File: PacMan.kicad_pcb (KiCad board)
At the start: 2 copper layers, 134.6 x 109.2 mm, 163 parts, among them J1 POWER+, J10 SEG+ CellMen, J13 AIR Left, J14 AIR Right, J2 POWER-, J4 Charge Detection, J5 SEG- CellMen, J6 BusBar Current Sensor, J7 Panel, J8 SLOOP, J9 GLV/CAN, K1 G5Q-1A4 DC24, K2 T9AS1D12-24, K3 T9AS1D12-24, Q1 DMN3730U, Q2 DMN3730U, Q4 DMP10H4D2S, Q5 DMP10H4D2S, U1 MCP9804, U10 LTC4151, U11 INA592, U12 MEF1S2405SP3C, U13 V7805-500, U14 Si8600AC, U15 Si8600AC, U16 TEC3-2419, U17 TEC3-2419, U18 AP2204K-5.0, U19 TLP293-4, U2 MCP9804, U21 Si8600AC, U22 AP2204K-5.0, U3 ADM6320, U4 MCP2551-I-SN, U5 ESP32_DEVKITC, U6 MCP23008, U7 BQ32002, U8 ACHS-7122, U9 PDQE10-Q48-S24-D, Y1 32K

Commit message: quick little routing thing
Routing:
- net /MCU/BTN_LEFT_MCU: track 44.4 -> 43.3 mm
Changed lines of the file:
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@@
-(kicad_pcb (version 20171130) (host pcbnew "(5.1.4)-1")
+(kicad_pcb (version 20171130) (host pcbnew "(5.1.5)-3")
   (general
     (thickness 1.6)
     (drawings 77)
-    (tracks 1638)
+    (tracks 1636)
     (zones 0)
     (modules 163)
@@
   )
   (setup
-    (last_trace_width 0.5)
+    (last_trace_width 0.25)
     (user_trace_width 0.5)
     (user_trace_width 1)
@@
     (add_net "Net-(ISO4-Pad1)")
     (add_net "Net-(ISO7-Pad1)")
-    (add_net "Net-(J10-Pad5)")
-    (add_net "Net-(J5-Pad5)")
-    (add_net "Net-(J6-Pad1)")
-    (add_net "Net-(J6-Pad6)")
-    (add_net "Net-(J7-Pad6)")
     (add_net "Net-(R2-Pad1)")
     (add_net "Net-(R24-Pad2)")
@@
     (add_net "Net-(R46-Pad1)")
     (add_net "Net-(R5-Pad1)")
-    (add_net "Net-(U1-Pad3)")
-    (add_net "Net-(U10-Pad8)")
-    (add_net "Net-(U11-Pad8)")
-    (add_net "Net-(U16-Pad3)")
-    (add_net "Net-(U17-Pad3)")
-    (add_net "Net-(U18-Pad4)")
-    (add_net "Net-(U2-Pad3)")
-    (add_net "Net-(U22-Pad4)")
-    (add_net "Net-(U4-Pad5)")
-    (add_net "Net-(U5-Pad16)")
-    (add_net "Net-(U5-Pad17)")
-    (add_net "Net-(U5-Pad18)")
-    (add_net "Net-(U5-Pad23)")
-    (add_net "Net-(U5-Pad24)")
-    (add_net "Net-(U5-Pad3)")
-    (add_net "Net-(U5-Pad33)")
-    (add_net "Net-(U5-Pad36)")
-    (add_net "Net-(U5-Pad37)")
-    (add_net "Net-(U5-Pad38)")
-    (add_net "Net-(U5-Pad4)")
-    (add_net "Net-(U6-Pad10)")
-    (add_net "Net-(U6-Pad11)")
-    (add_net "Net-(U6-Pad7)")
-    (add_net "Net-(U7-Pad7)")
-    (add_net "Net-(U9-Pad6)")
   )
   (net_class "TSV Pre Fuse" ""
@@
   (segment (start 191.77 113.03) (end 186.69 113.03) (width 0.25) (layer F.Cu) (net 6))
   (via (at 186.69 113.03) (size 0.8) (drill 0.4) (layers F.Cu B.Cu) (net 6))
-  (segment (start 156.21 107.95) (end 156.21 109.053086) (width 0.25) (layer F.Cu) (net 6))
-  (segment (start 156.21 109.053086) (end 156.21 109.22) (width 0.25) (layer F.Cu) (net 6))
-  (segment (start 156.21 109.22) (end 158.75 111.76) (width 0.25) (layer F.Cu) (net 6))
-  (via (at 160.02 111.76) (size 0.8) (drill 0.4) (layers F.Cu B.Cu) (net 6))
-  (segment (start 158.75 111.76) (end 160.02 111.76) (width 0.25) (layer F.Cu) (net 6))
-  (via (at 162.56 111.125) (size 0.8) (drill 0.4) (layers F.Cu B.Cu) (net 6))
-  (segment (start 160.02 111.76) (end 161.925 111.76) (width 0.25) (layer B.Cu) (net 6))
-  (segment (start 161.925 111.76) (end 162.56 111.125) (width 0.25) (layer B.Cu) (net 6))
-  (via (at 170.18 111.125) (size 0.8) (drill 0.4) (layers F.Cu B.Cu) (net 6))
-  (segment (start 162.56 111.125) (end 170.18 111.125) (width 0.25) (layer F.Cu) (net 6))
-  (via (at 172.72 111.125) (size 0.8) (drill 0.4) (layers F.Cu B.Cu) (net 6))
-  (segment (start 170.18 111.125) (end 172.72 111.125) (width 0.25) (layer B.Cu) (net 6))
-  (segment (start 173.355 110.49) (end 172.72 111.125) (width 0.25) (layer F.Cu) (net 6))
-  (segment (start 181.61 110.49) (end 173.355 110.49) (width 0.25) (layer F.Cu) (net 6))
   (segment (start 184.15 110.49) (end 186.69 113.03) (width 0.25) (layer B.Cu) (net 6))
   (via (at 181.61 110.49) (size 0.8) (drill 0.4) (layers F.Cu B.Cu) (net 6))
   (segment (start 181.61 110.49) (end 184.15 110.49) (width 0.25) (layer B.Cu) (net 6))
+  (via (at 172.72 110.49) (size 0.8) (drill 0.4) (layers F.Cu B.Cu) (net 6))
+  (segment (start 181.61 110.49) (end 172.72 110.49) (width 0.25) (layer F.Cu) (net 6))
+  (segment (start 170.18 110.49) (end 172.72 110.49) (width 0.25) (layer B.Cu) (net 6))
+  (via (at 170.18 110.49) (size 0.8) (drill 0.4) (layers F.Cu B.Cu) (net 6))
+  (segment (start 162.56 110.49) (end 170.18 110.49) (width 0.25) (layer F.Cu) (net 6))
+  (via (at 162.56 110.49) (size 0.8) (drill 0.4) (layers F.Cu B.Cu) (net 6))
+  (via (at 160.02 110.49) (size 0.8) (drill 0.4) (layers F.Cu B.Cu) (net 6))
+  (segment (start 162.56 110.49) (end 160.02 110.49) (width 0.25) (layer B.Cu) (net 6))
+  (segment (start 156.21 109.053086) (end 156.21 107.95) (width 0.25) (layer F.Cu) (net 6))
+  (segment (start 156.21 109.22) (end 156.21 109.053086) (width 0.25) (layer F.Cu) (net 6))
+  (segment (start 160.02 110.49) (end 157.48 110.49) (width 0.25) (layer F.Cu) (net 6))
+  (segment (start 157.48 110.49) (end 156.21 109.22) (width 0.25) (layer F.Cu) (net 6))
   (via (at 191.77 116.84) (size 0.8) (drill 0.4) (layers F.Cu B.Cu) (net 7))
   (segment (start 193.285 116.84) (end 191.77 116.84) (width 0.25) (layer B.Cu) (net 7) (status 10))

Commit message: a bit of dimensioning
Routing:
- net /Power/PACK_FUSED_CS: track 17.1 -> 19.0 mm
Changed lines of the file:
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@@
   (general
     (thickness 1.6)
-    (drawings 77)
-    (tracks 1636)
+    (drawings 79)
+    (tracks 1638)
     (zones 0)
     (modules 163)
@@
   )
   (setup
-    (last_trace_width 0.25)
+    (last_trace_width 0.5)
     (user_trace_width 0.5)
     (user_trace_width 1)
@@
     )
   )
-  (dimension 4.445 (width 0.12) (layer Dwgs.User)
-    (gr_text "4.445 mm" (at 119.38 60.6425 90) (layer Dwgs.User)
-      (effects (font (size 1 1) (thickness 0.15)))
-    )
-    (feature1 (pts (xy 109.22 58.42) (xy 118.696421 58.42)))
-    (feature2 (pts (xy 109.22 62.865) (xy 118.696421 62.865)))
-    (crossbar (pts (xy 118.11 62.865) (xy 118.11 58.42)))
-    (arrow1a (pts (xy 118.11 58.42) (xy 118.696421 59.546504)))
-    (arrow1b (pts (xy 118.11 58.42) (xy 117.523579 59.546504)))
-    (arrow2a (pts (xy 118.11 62.865) (xy 118.696421 61.738496)))
-    (arrow2b (pts (xy 118.11 62.865) (xy 117.523579 61.738496)))
+  (dimension 6.35 (width 0.12) (layer Dwgs.User)
+    (gr_text "6.350 mm" (at 122.555 81.914999) (layer Dwgs.User)
+      (effects (font (size 0.75 0.75) (thickness 0.15)))
+    )
+    (feature1 (pts (xy 125.73 76.835) (xy 125.73 81.23142)))
+    (feature2 (pts (xy 119.38 76.835) (xy 119.38 81.23142)))
+    (crossbar (pts (xy 119.38 80.644999) (xy 125.73 80.644999)))
+    (arrow1a (pts (xy 125.73 80.644999) (xy 124.603496 81.23142)))
+    (arrow1b (pts (xy 125.73 80.644999) (xy 124.603496 80.058578)))
+    (arrow2a (pts (xy 119.38 80.644999) (xy 120.506504 81.23142)))
+    (arrow2b (pts (xy 119.38 80.644999) (xy 120.506504 80.058578)))
+  )
+  (dimension 5.461 (width 0.12) (layer Dwgs.User)
+    (gr_text "5.461 mm" (at 164.2745 76.454) (layer Dwgs.User)
+      (effects (font (size 0.75 0.75) (thickness 0.15)))
+    )
+    (feature1 (pts (xy 161.544 70.485) (xy 161.544 75.770421)))
+    (feature2 (pts (xy 167.005 70.485) (xy 167.005 75.770421)))
+    (crossbar (pts (xy 167.005 75.184) (xy 161.544 75.184)))
+    (arrow1a (pts (xy 161.544 75.184) (xy 162.670504 74.597579)))
+    (arrow1b (pts (xy 161.544 75.184) (xy 162.670504 75.770421)))
+    (arrow2a (pts (xy 167.005 75.184) (xy 165.878496 74.597579)))
+    (arrow2b (pts (xy 167.005 75.184) (xy 165.878496 75.770421)))
+  )
+  (dimension 5.715 (width 0.12) (layer Dwgs.User)
+    (gr_text "5.715 mm" (at 118.745 61.2775 270) (layer Dwgs.User)
+      (effects (font (size 0.75 0.75) (thickness 0.15)))
+    )
+    (feature1 (pts (xy 111.76 64.135) (xy 118.061421 64.135)))
+    (feature2 (pts (xy 111.76 58.42) (xy 118.061421 58.42)))
+    (crossbar (pts (xy 117.475 58.42) (xy 117.475 64.135)))
+    (arrow1a (pts (xy 117.475 64.135) (xy 116.888579 63.008496)))
+    (arrow1b (pts (xy 117.475 64.135) (xy 118.061421 63.008496)))
+    (arrow2a (pts (xy 117.475 58.42) (xy 116.888579 59.546504)))
+    (arrow2b (pts (xy 117.475 58.42) (xy 118.061421 59.546504)))
   )
   (gr_line (start 92.075 53.975) (end 92.075 52.705) (layer F.SilkS) (width 0.12))
@@
   (segment (start 153.67 76.2) (end 152.4 77.47) (width 0.5) (layer F.Cu) (net 12))
   (segment (start 155.82 76.2) (end 153.67 76.2) (width 0.5) (layer F.Cu) (net 12) (status 10))
-  (segment (start 147.955 81.915) (end 152.4 77.47) (width 0.5) (layer F.Cu) (net 12) (status 10))
   (segment (start 149.0075 80.8625) (end 147.955 81.915) (width 0.5) (layer B.Cu) (net 12) (status 20))
   (segment (start 149.0075 78.74) (end 149.0075 80.8625) (width 0.5) (layer B.Cu) (net 12) (status 10))
@@
   (segment (start 154.645 73.39) (end 154.645 74) (width 0.25) (layer F.Cu) (net 12) (status 10))
   (segment (start 154.645 74) (end 155.82 75.175) (width 0.25) (layer F.Cu) (net 12))
+  (segment (start 147.955 81.915) (end 147.955 78.74) (width 0.5) (layer F.Cu) (net 12))
+  (segment (start 149.225 77.47) (end 152.4 77.47) (width 0.5) (layer F.Cu) (net 12))
+  (segment (start 147.955 78.74) (end 149.225 77.47) (width 0.5) (layer F.Cu) (net 12))
   (segment (start 149.0075 102.235) (end 140.335 102.235) (width 0.25) (layer B.Cu) (net 13) (status 30))
   (segment (start 139.065 100.965) (end 140.335 102.235) (width 0.5) (layer F.Cu) (net 13) (status 20))

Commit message: Maybe final version of PacMan
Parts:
- added C42: C, Capacitor_SMD:C_0805_2012Metric_Pad1.15x1.40mm_HandSolder, F.Cu at (122.2, 97.2)
- added R48: R, Resistor_SMD:R_0805_2012Metric_Pad1.15x1.40mm_HandSolder, F.Cu at (122.2, 99.1)
- moved R33 7.00 mm to (122.2, 101.0), turned to 180 degrees
- moved R35 5.21 mm to (122.2, 95.2), turned to 180 degrees
- turned TP5 to 180 degrees
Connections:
- ISO2 pad 4: /~CHRG_DETECT -> Net-(ISO2-Pad4)
- R33 pad 1: /~CHRG_DETECT -> Net-(ISO2-Pad4)
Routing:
- net /AIRS+: track 159.7 -> 171.6 mm
- net Net-(ISO2-Pad4): track 0.00 -> 11.0 mm
- net /~CHRG_DETECT: track 40.5 -> 51.4 mm
- net /LV_3V3: track 355.5 -> 359.7 mm
- net /AIRS-: track 183.4 -> 179.6 mm
- net Net-(ISO4-Pad1): track 3.07 -> 1.91 mm
- net /GLV_RTN: track 147.8 -> 148.8 mm
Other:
- board text added: "HV"
- board text added: "LV"
- board text removed: "High Voltage"

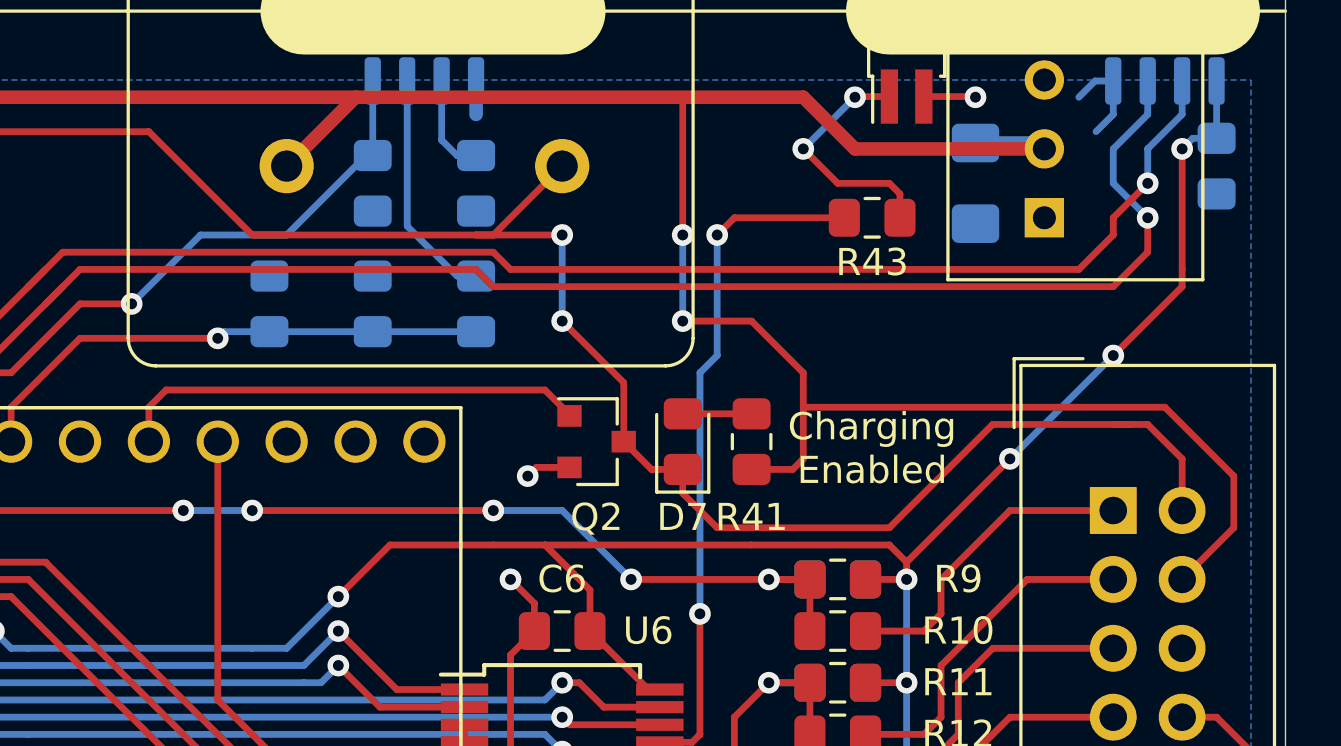
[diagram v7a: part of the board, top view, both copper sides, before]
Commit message: Added comments to the schematic, changed some formatting, made the charge LED a high side switch, some small value changes, layout update
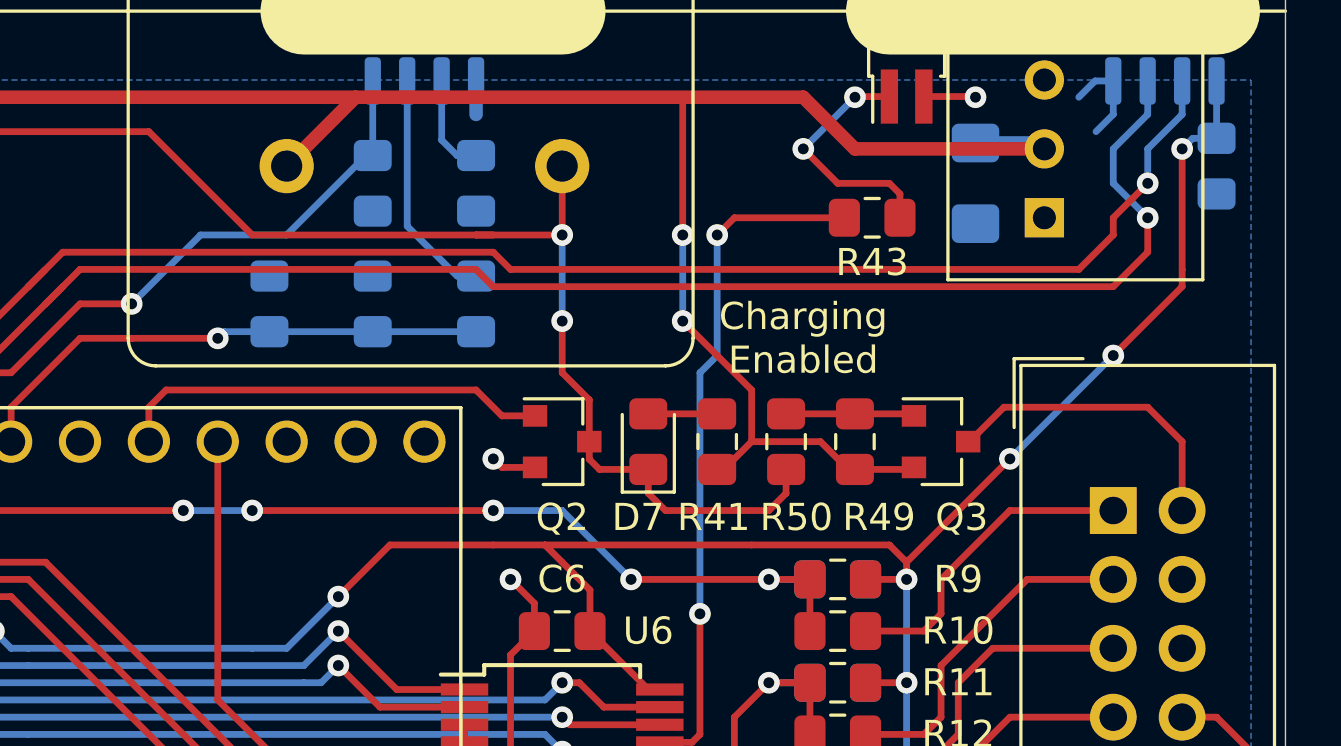
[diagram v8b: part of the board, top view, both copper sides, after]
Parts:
- added G***: LOGO, Lafayette_Electric_Car_Footprints:pacman_github_link, B.Cu at (148.0, 63.5)
- added Q3: DMP10H4D2S, Package_TO_SOT_SMD:SOT-23, F.Cu at (198.1, 108.0)
- added R49: 4.7k, Resistor_SMD:R_0805_2012Metric_Pad1.15x1.40mm_HandSolder, F.Cu at (194.9, 108.0)
- added R50: 4.7k, Resistor_SMD:R_0805_2012Metric_Pad1.15x1.40mm_HandSolder, F.Cu at (192.4, 108.0)
- C40: value C -> 1u/50V
- C41: value 0.1u/50V -> 1u/50V
- R34: value 500 -> 470
- moved D7 1.27 mm to (187.3, 108.0)
- moved Q2 1.27 mm to (184.2, 108.0)
- moved R41 1.27 mm to (189.9, 108.0)
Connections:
- net /MCU/LED1 renamed /MCU/LED_G
- net /MCU/LED2 renamed /MCU/LED_O
- D4 pad 2: /CHRG_LED -> Net-(D4-Pad2)
- D7 pad 1: /CHRG_LED -> Net-(D4-Pad2)
- J7 pad 4: /LV_24V -> (no net)
- K2 pad 2: /CHRG_LED -> Net-(D4-Pad2)
- K3 pad 2: /CHRG_LED -> Net-(D4-Pad2)
- Q2 pad 3: /CHRG_LED -> Net-(D4-Pad2)
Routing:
- net /CHRG_LED: track 128.6 -> 11.5 mm, vias 2 -> 0
- net Net-(D4-Pad2): track 0.00 -> 110.3 mm, vias 0 -> 2
- net /LV_24V: track 363.7 -> 345.4 mm
- net Net-(Q3-Pad1): track 0.00 -> 4.75 mm
- net /CHRG_EN: track 17.5 -> 16.2 mm
